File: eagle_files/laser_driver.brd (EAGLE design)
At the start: 100 x 50 mm, 40 parts, among them IC1 OKR-T/50-W12-C, IC2 7805, IC3 TLC272, J1 74650073R, J2 74650073R, J3 74650073R

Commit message: Cleaned up brd after cosmetic changes
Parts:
- moved IC1 47.7 mm to (55.9, 23.0)
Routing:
- net 5V: track 32.7 -> 40.6 mm
- net ENABLE: track 30.9 -> 35.5 mm
- net TRIM: track 12.1 -> 15.6 mm
- net N$4: track 36.4 -> 36.8 mm, vias 0 -> 10
- added copper zone on layer 1, net N$4
- added copper zone on layer 16, net N$4
- removed copper zone on layer 1, net N$7
- removed copper zone on layer 16, net N$7
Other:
- board text added: "marco@reps.cc September 2018"

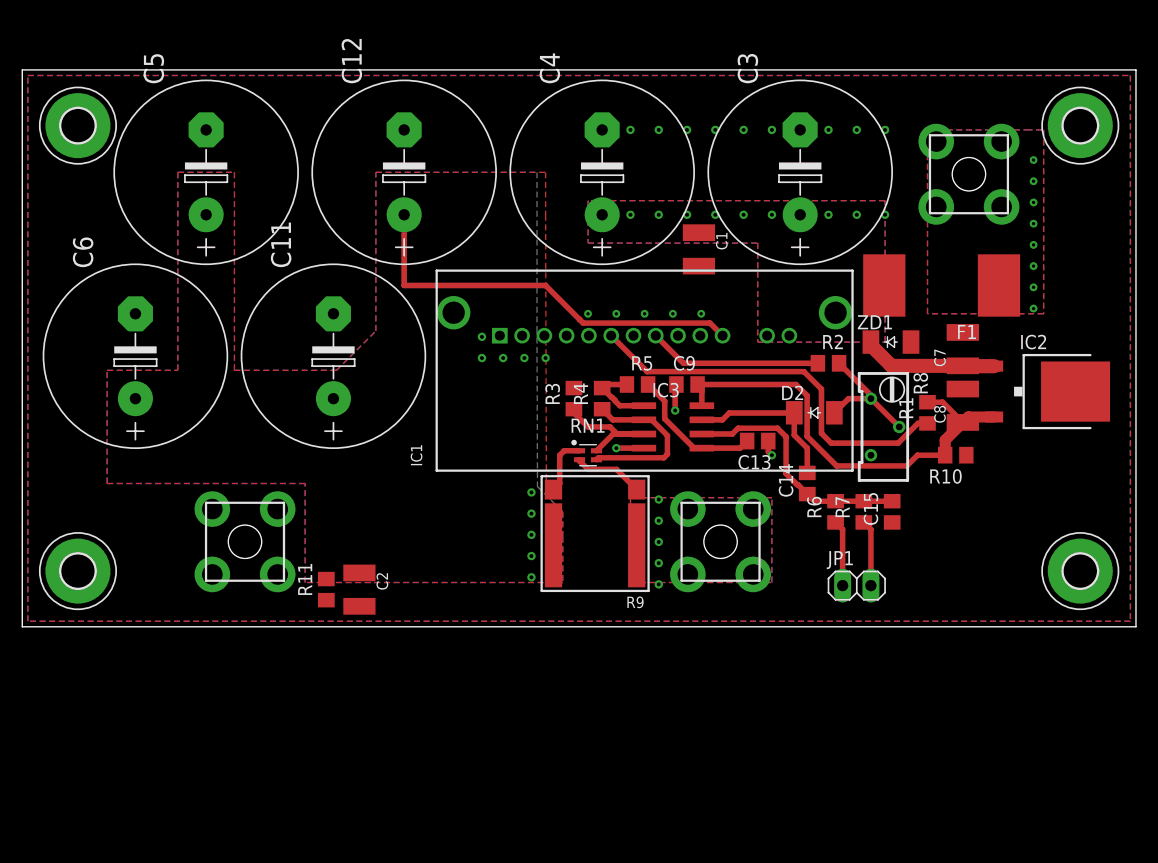
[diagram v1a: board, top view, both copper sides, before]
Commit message: Improved stability, removed useless caps
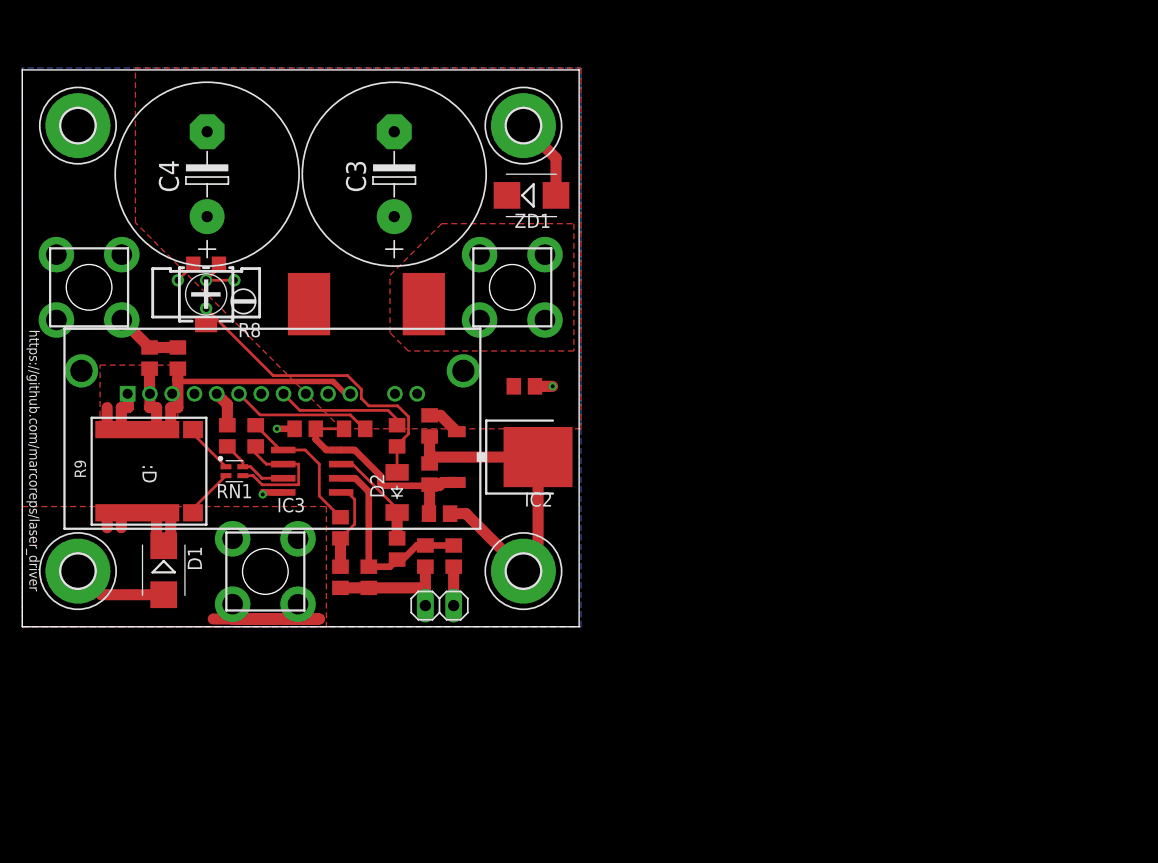
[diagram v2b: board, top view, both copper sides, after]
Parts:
- removed C11, C12, C5, C6: 4700 µF, resistor:E7,5-16
- added D1: ES2D, diode:SMB
- added R12: (no value), rcl:RTRIM4G/J
- C1, C2, C7, C8: device resistor:C1210K -> rcl:C0805
- C13: value 22 µF -> 100 nF
- C14: value 22µF -> 4.7µF
- R6: value 10k -> 2k
- ZD1: value CGRM4001-G -> ES2D; device diode:SOD-123_MINI-SMA -> diode:SMB
- moved R8 61.1 mm to (16.5, 31.1), turned to 90 degrees
- moved F1 51.7 mm to (30.9, 29.0)
- moved R1 51.5 mm to (29.8, 17.8), turned to 180 degrees
- moved H3 50.0 mm to (45.0, 45.0)
- moved H4 50.0 mm to (45.0, 5.00)
- moved IC2 48.6 mm to (43.8, 15.2)
- moved C7 48.4 mm to (36.6, 18.0), turned to 270 degrees
- moved C8 48.3 mm to (36.6, 13.7)
- moved R10 46.7 mm to (37.5, 10.2)
- moved R7 44.8 mm to (31.1, 4.45)
- moved J1 42.2 mm to (44.0, 30.5)
- moved C15 42.1 mm to (36.2, 6.35)
- moved J3 41.0 mm to (21.8, 4.96)
- moved R9 40.4 mm to (11.4, 14.0), turned to 0 degrees
- moved C13 39.4 mm to (28.6, 4.45), turned to 90 degrees
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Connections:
- net GND: now also D1.A, IC1.14, IC1.15, R12.3; no longer C11.-, C12.-, C5.-, C6.-
- net N$1: now also D1.C
- net N$2: now also R12.1, R12.2
- net N$4: no longer C11.+, C12.+, C5.+, C6.+
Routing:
- net GND: track 12.2 -> 77.0 mm, vias 17 -> 3
- net N$1: track 0.00 -> 34.8 mm, vias 5 -> 0
- net N$2: track 11.8 -> 36.6 mm, vias 0 -> 1
- net ENABLE: track 35.5 -> 12.6 mm
- net 5V: track 40.6 -> 21.1 mm
- net VIN: track 12.1 -> 3.05 mm, vias 9 -> 0
- net N$119: track 6.80 -> 12.7 mm
- net N$299: track 14.4 -> 9.35 mm
- net N$13: track 11.1 -> 6.46 mm
- net N$298: track 12.5 -> 8.03 mm
- net TRIM: track 15.6 -> 11.7 mm
- net N$301: track 21.9 -> 18.1 mm
- net CV: track 5.94 -> 3.50 mm
- net N$118: track 15.1 -> 12.8 mm
- net N$12: track 6.31 -> 4.56 mm
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- removed copper zone on layer 1, net GND
- removed copper zone on layer 16, net N$1
- removed copper zone on layer 16, net N$4
- removed copper zone on layer 16, net N$5
- removed copper zone on layer 16, net VIN
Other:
- board size 100 x 50 mm -> 50 x 50 mm
- board text added: ":D"
- board text added: "https://github.com/marcoreps/laser_driver"

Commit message: Improved silk screen
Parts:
- C9: value 100 nF -> 100nF
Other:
- board text added: "GND, CV ->"
- board text removed: "<- CV, GND"
- board text removed: "marco@reps.cc September 2018"

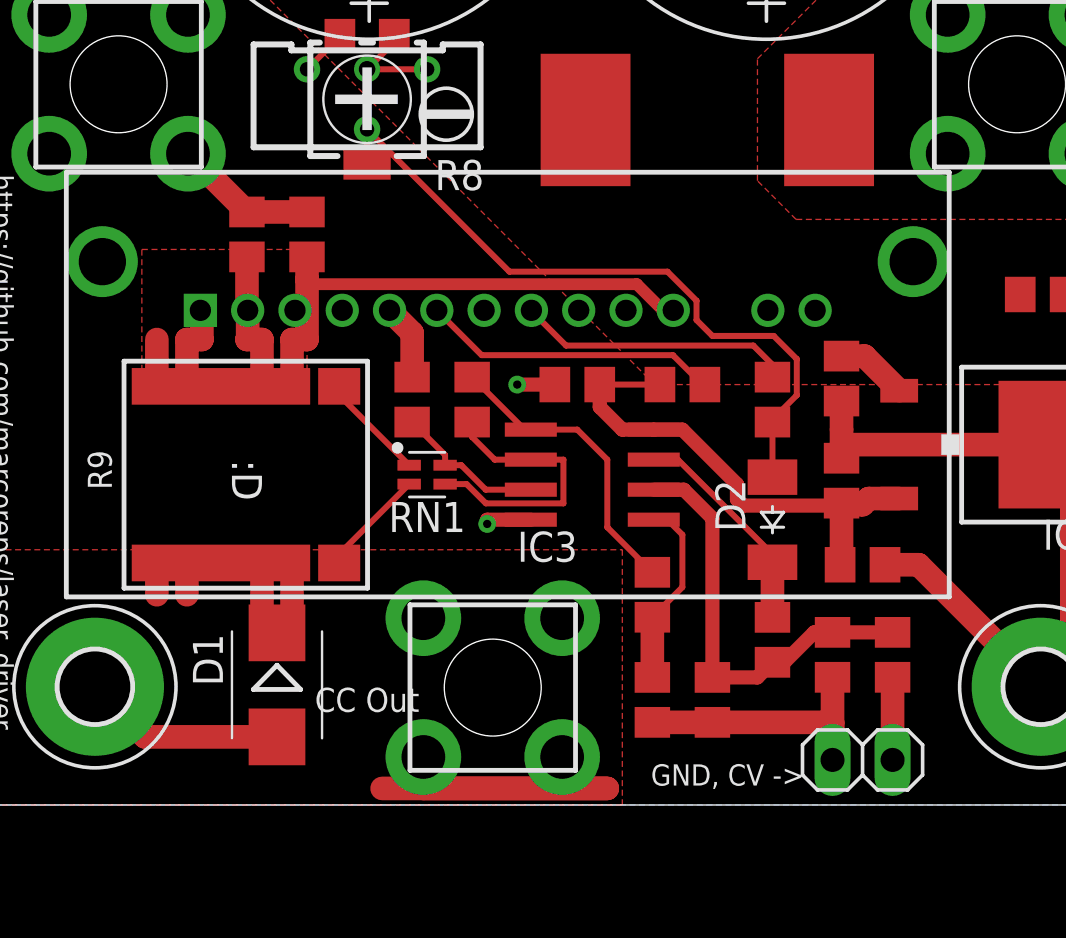
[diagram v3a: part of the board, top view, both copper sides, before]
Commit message: Minor changes in component placement after assembly
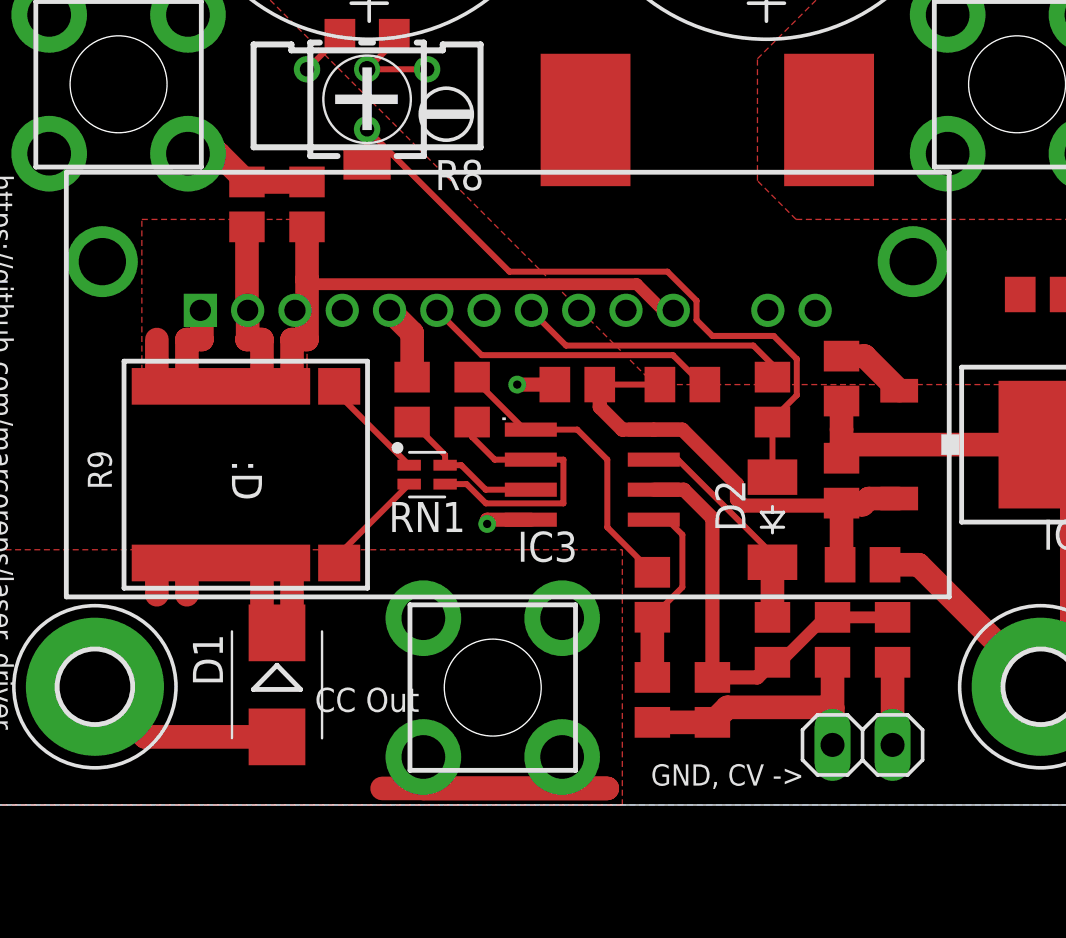
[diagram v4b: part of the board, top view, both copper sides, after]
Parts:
- C13: value 100 nF -> 100nF
- moved C2 1.27 mm to (14.0, 25.4)
- moved R11 1.27 mm to (11.4, 25.4)
- moved C15 0.64 mm to (36.2, 6.99)
- moved R6 0.64 mm to (38.7, 6.99)
- moved JP1 0.64 mm to (37.5, 2.54)
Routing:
- net N$4: track 35.3 -> 37.8 mm
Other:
- board text added: "."
